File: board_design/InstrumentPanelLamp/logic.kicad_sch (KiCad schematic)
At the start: 30 parts, among them Q10 BSD840N, Q2 BC327, Q8 BSD840N, Q9 BSD840N, U1 LT3092xST

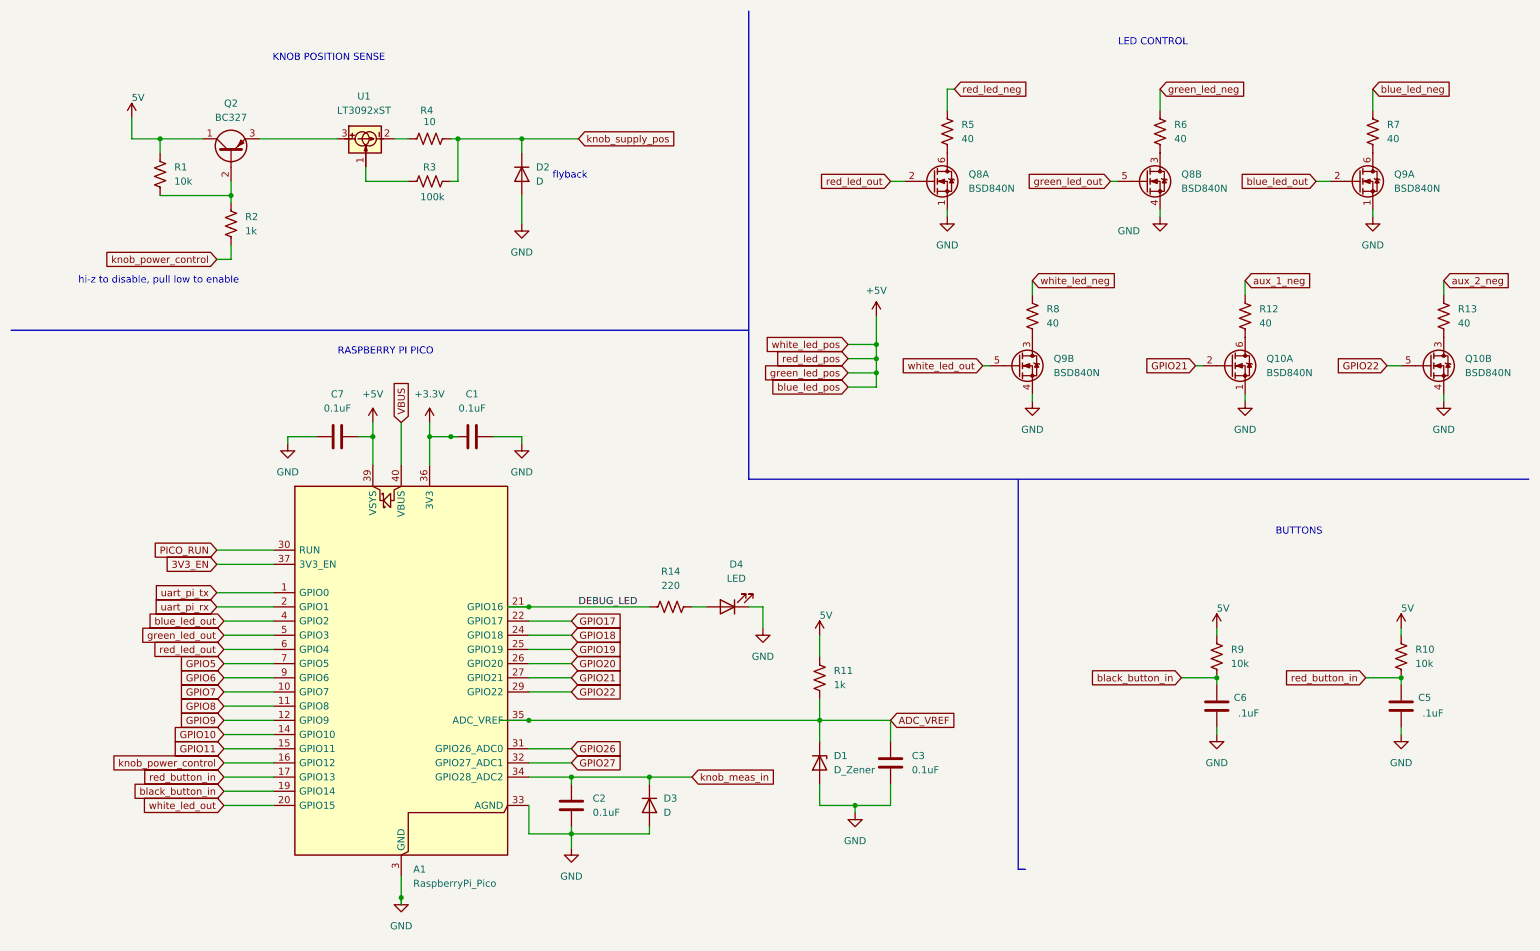
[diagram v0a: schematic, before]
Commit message: Complete initial version of Arduino code and initial PCB placement
The arduino sketch is now as functional as the old version was.
The kicab pcb file has the initial placement of components done as
well using the updated Arduino pro mini as the MCU.
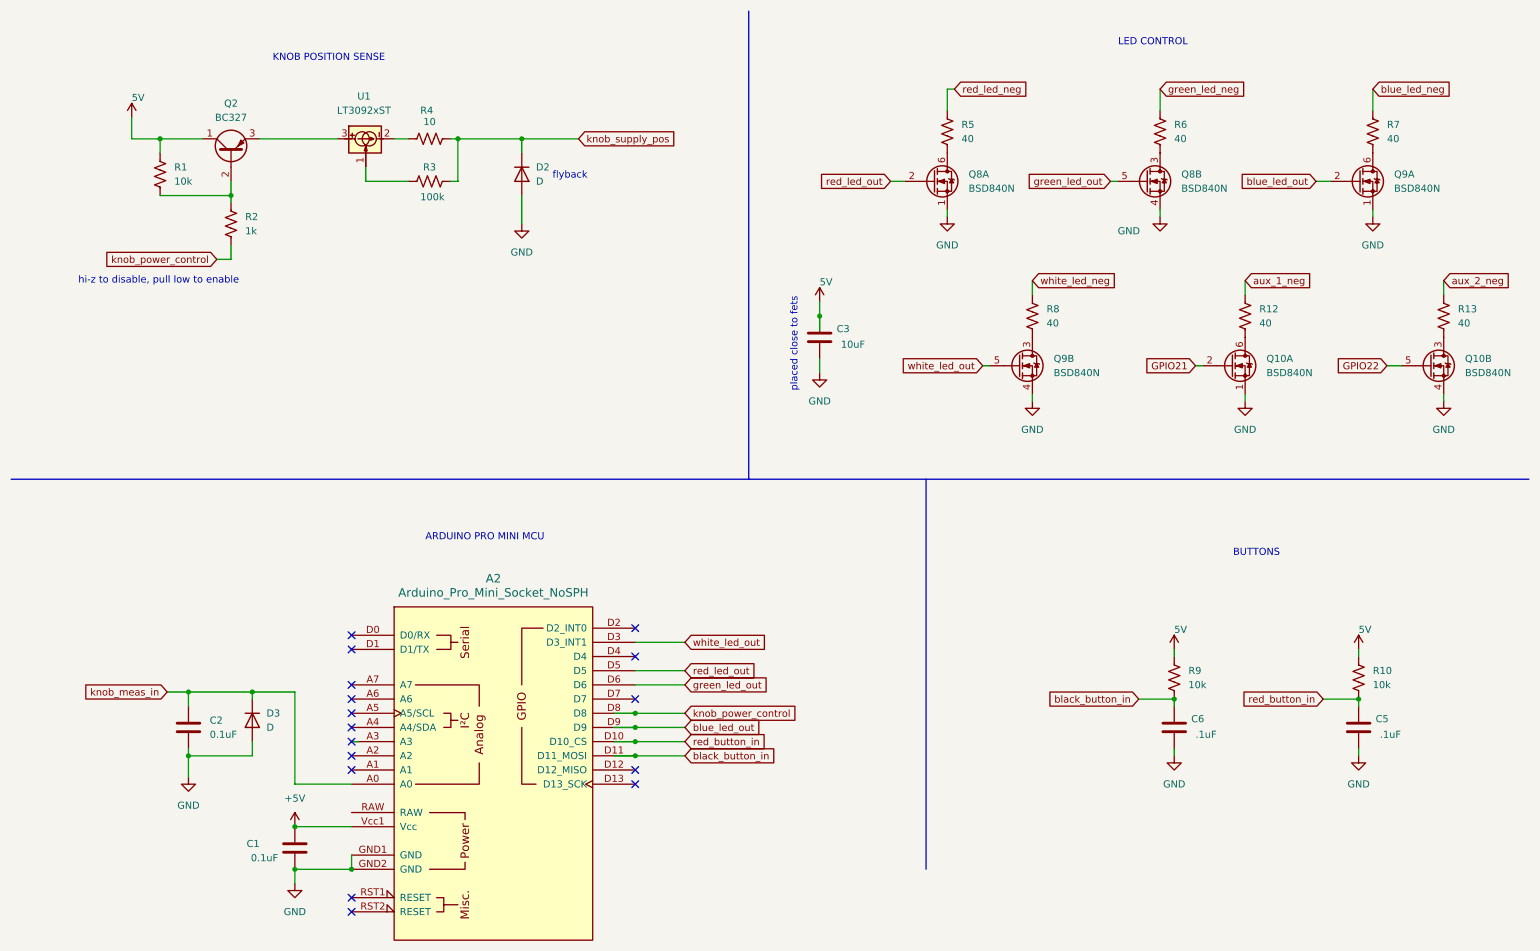
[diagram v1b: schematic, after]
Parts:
- removed A1: RaspberryPi_Pico, Module:RaspberryPi_Pico_Common_Unspecified, symbol MCU_Module:RaspberryPi_Pico
- removed C7: 0.1uF, Capacitor_SMD:C_0805_2012Metric_Pad1.18x1.45mm_HandSolder, symbol Device:C
- removed D1: D_Zener, Diode_SMD:D_0805_2012Metric_Pad1.15x1.40mm_HandSolder, symbol Device:D_Zener
- removed D4: LED, Diode_SMD:D_0805_2012Metric_Pad1.15x1.40mm_HandSolder, symbol Device:LED
- removed R11: 1k, Resistor_SMD:R_0805_2012Metric_Pad1.20x1.40mm_HandSolder, symbol Device:R_US
- removed R14: 220, Resistor_SMD:R_0805_2012Metric_Pad1.20x1.40mm_HandSolder, symbol Device:R_US
- added A2: Arduino_Pro_Mini_Socket_NoSPH, PCM_arduino-library:Arduino_Pro_Mini_Socket_NoSPH, symbol PCM_arduino-library:Arduino_Pro_Mini_Socket_NoSPH
- C3: value 0.1uF -> 10uF
- R12, R13, R4, R5, R6, R7, R8: footprint Resistor_THT:R_Axial_DIN0207_L6.3mm_D2.5mm_P7.62mm_Horizontal -> Resistor_SMD:R_0805_2012Metric_Pad1.20x1.40mm_HandSolder
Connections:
- net +3.3V is gone; now on net +5V: C1.1
- net ADC_VREF is gone; now on net 5V: C3.2
- net +5V: now also A2.Vcc1 (Vcc)
- net GND: now also A2.GND1 (GND), A2.GND2 (GND)
- net black_button_in: now also A2.D11 (D11_MOSI)
- net blue_led_out: now also A2.D9
- net green_led_out: now also A2.D6
- net knob_meas_in: now also A2.A0
- net knob_power_control: now also A2.D8
- net red_button_in: now also A2.D10 (D10_CS)
- net red_led_out: now also A2.D5
- net white_led_out: now also A2.D3 (D3_INT1)
- no-connect marks 0 -> 16
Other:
- note added: "ARDUINO PRO MINI MCU"
- note added: "placed close to fets"
- note removed: "RASPBERRY PI PICO"
- moved on the sheet: C1, C2, C5, C6, D3, R10, R9

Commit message: board: Update board/sch design files with 3d model changes
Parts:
- removed Q2: BC327, Package_TO_SOT_THT:TO-92_Inline, symbol Transistor_BJT:BC327
- added Q1: DMG2302U, Package_TO_SOT_SMD:SOT-23, symbol Transistor_FET:DMG2302U
- D2, D3: footprint Diode_THT:D_A-405_P7.62mm_Horizontal -> Diode_SMD:D_SMA_Handsoldering
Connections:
- net 5V is gone; now on net +5V: C3.2, R1.1, R10.1, R9.1
- net GPIO21 is gone; now on net aux1: Q10.2 (G)
- net GPIO22 is gone; now on net aux2: Q10.5 (G)
- net +5V: now also Q1.3 (D)
- net pch_gate: now reaches R1.2, R2.1
- net pch_gate: now also Q1.1 (G)
- net at U1.3: now also Q1.2 (S)
- net aux1: now reaches A2.D12 (D12_MISO)
- net aux2: now reaches A2.D13 (D13_SCK)
- no-connect marks 16 -> 14
